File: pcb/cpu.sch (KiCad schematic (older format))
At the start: 36 parts, among them P27 BDM, P57 TX1, P58 RX1, P59 TX, P60 RX, P64 RXCAN0, P65 TXCAN0, U1 MC9S12XDP512, X1 16MHz

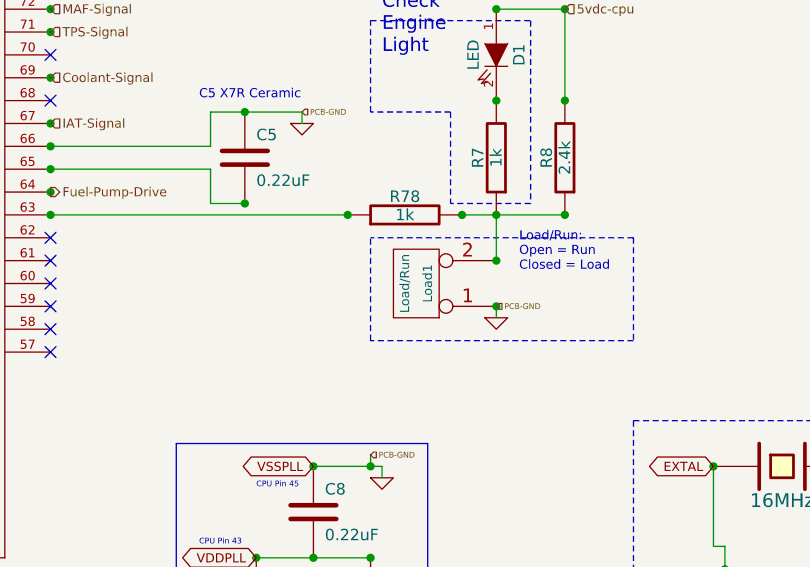
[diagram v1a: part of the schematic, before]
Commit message: Updated TODO.md for R20 and R23 footprint error.
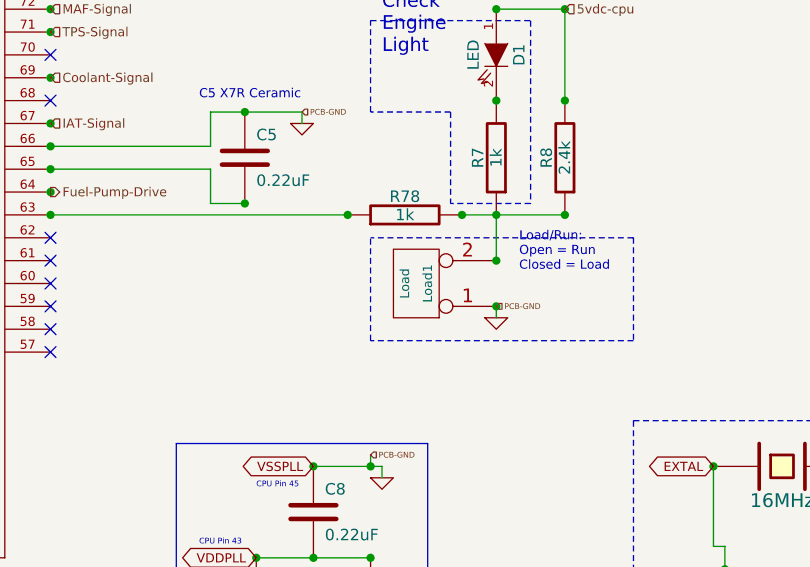
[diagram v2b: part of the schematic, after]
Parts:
- Load1: value Load/Run -> Load
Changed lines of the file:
@@
-EESchema Schematic File Version 2  date Sun 12 May 2013 04:07:09 PM EDT
+EESchema Schematic File Version 2  date Sun 12 May 2013 06:47:41 PM EDT
 LIBS:opto
 LIBS:power
@@
 Title "Jaguar PCB for FreeEMS"
 Date "12 may 2013"
-Rev "0.4-alpha"
-Comp "git hash: 3495ad36ad"
+Rev "0.6-alpha"
+Comp "git hash: xxxxxxxxxx"
 Comment1 ""
 Comment2 ""
@@
 P 8600 5150
 F 0 "Load1" V 8550 5150 40  0000 C CNN
-F 1 "Load/Run" V 8650 5150 40  0000 C CNN
+F 1 "Load" V 8650 5150 40  0000 C CNN
 	1    8600 5150
 	-1   0    0    1

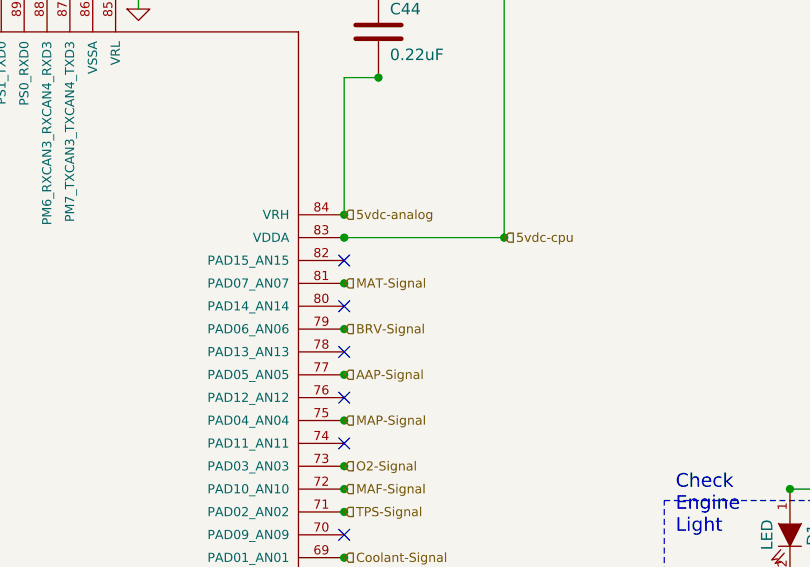
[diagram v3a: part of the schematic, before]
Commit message: Rename MAT to SPR.
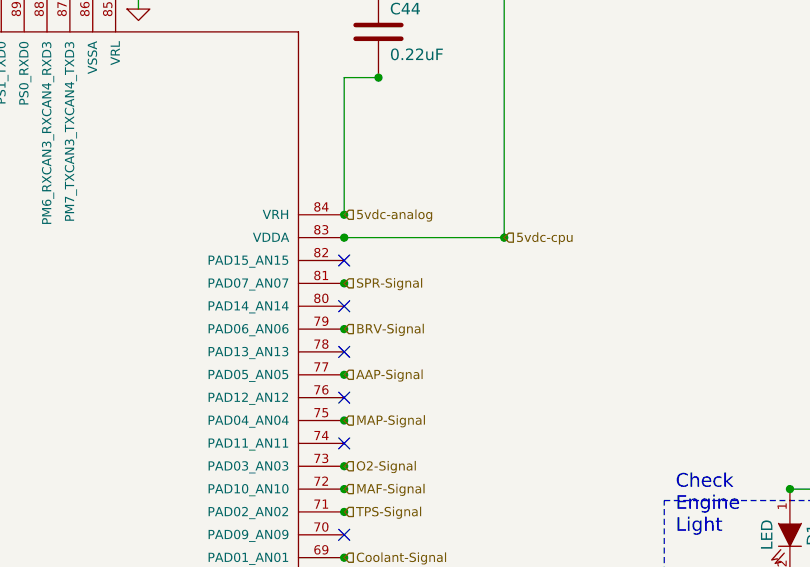
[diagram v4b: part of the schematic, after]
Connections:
- net labels added: SPR-Signal
- net labels removed: MAT-Signal
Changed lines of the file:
@@
-EESchema Schematic File Version 2  date Mon 13 May 2013 11:53:03 AM EDT
+EESchema Schematic File Version 2  date Mon 13 May 2013 12:23:58 PM EDT
 LIBS:opto
 LIBS:power
@@
 MAF-Signal
 Text HLabel 7000 3050 2    40   Input ~ 0
-MAT-Signal
+SPR-Signal
 Text HLabel 7000 3250 2    40   Input ~ 0
 BRV-Signal

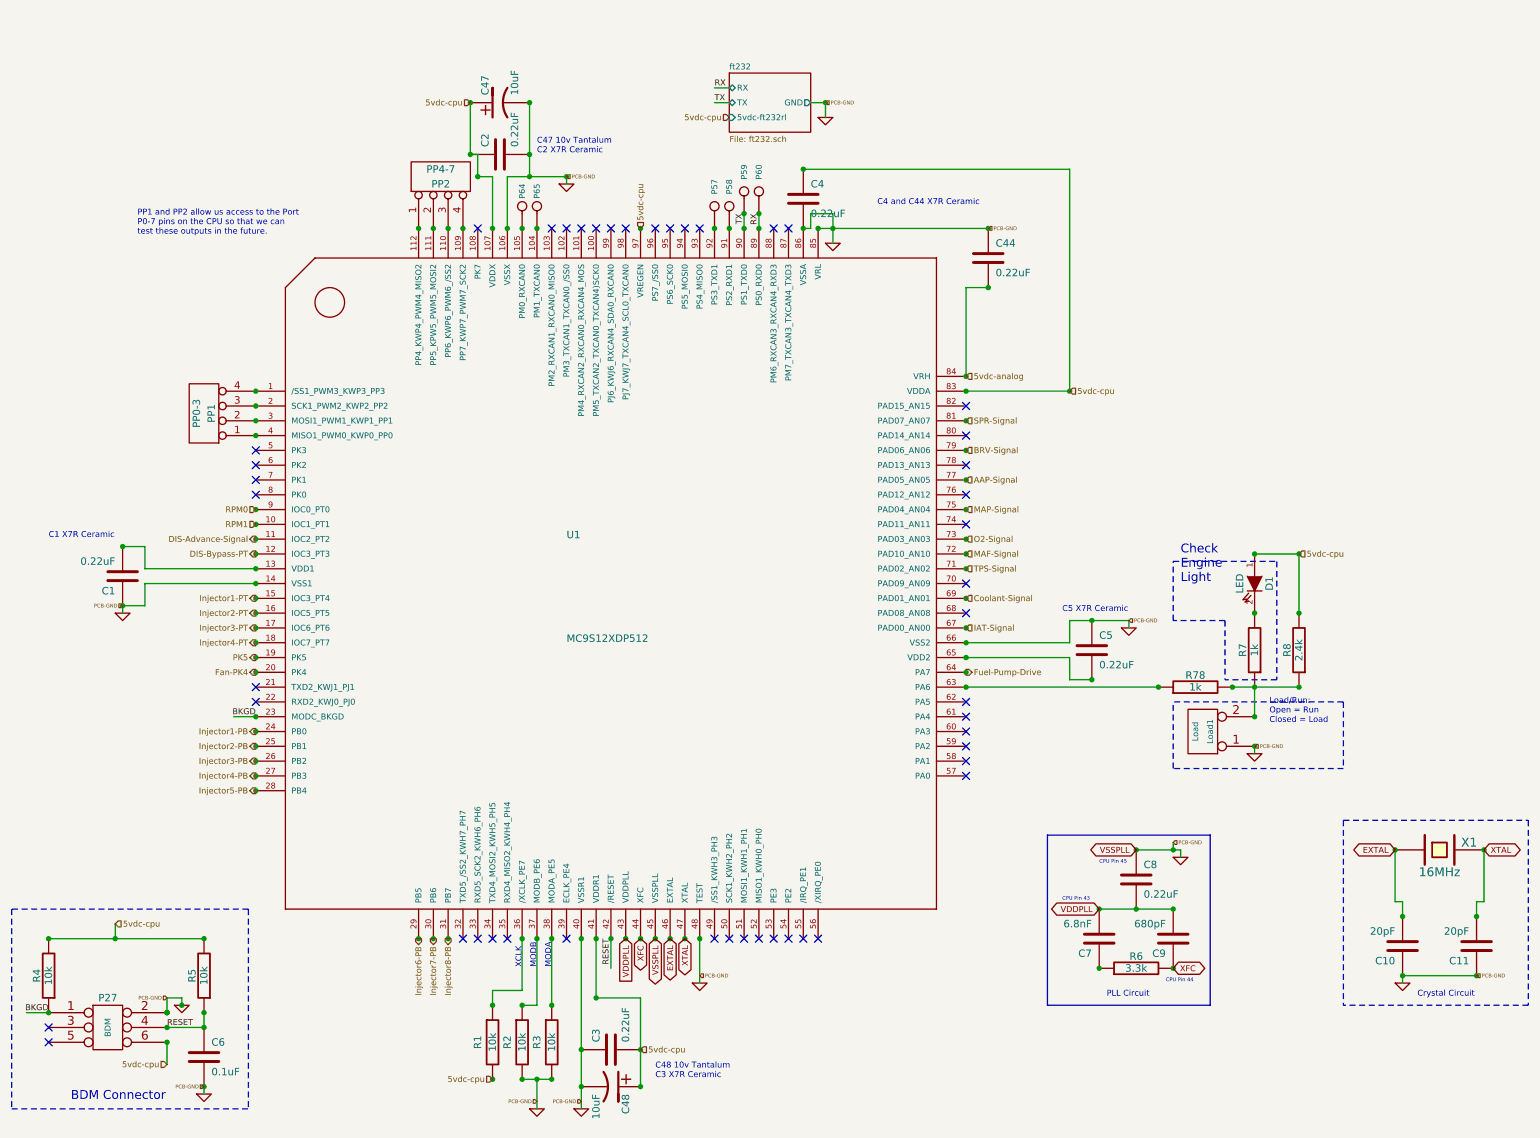
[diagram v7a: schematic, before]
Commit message: Made the CANRX0/CANTX0 into a 0.100" header so that a add-on card could be created later.
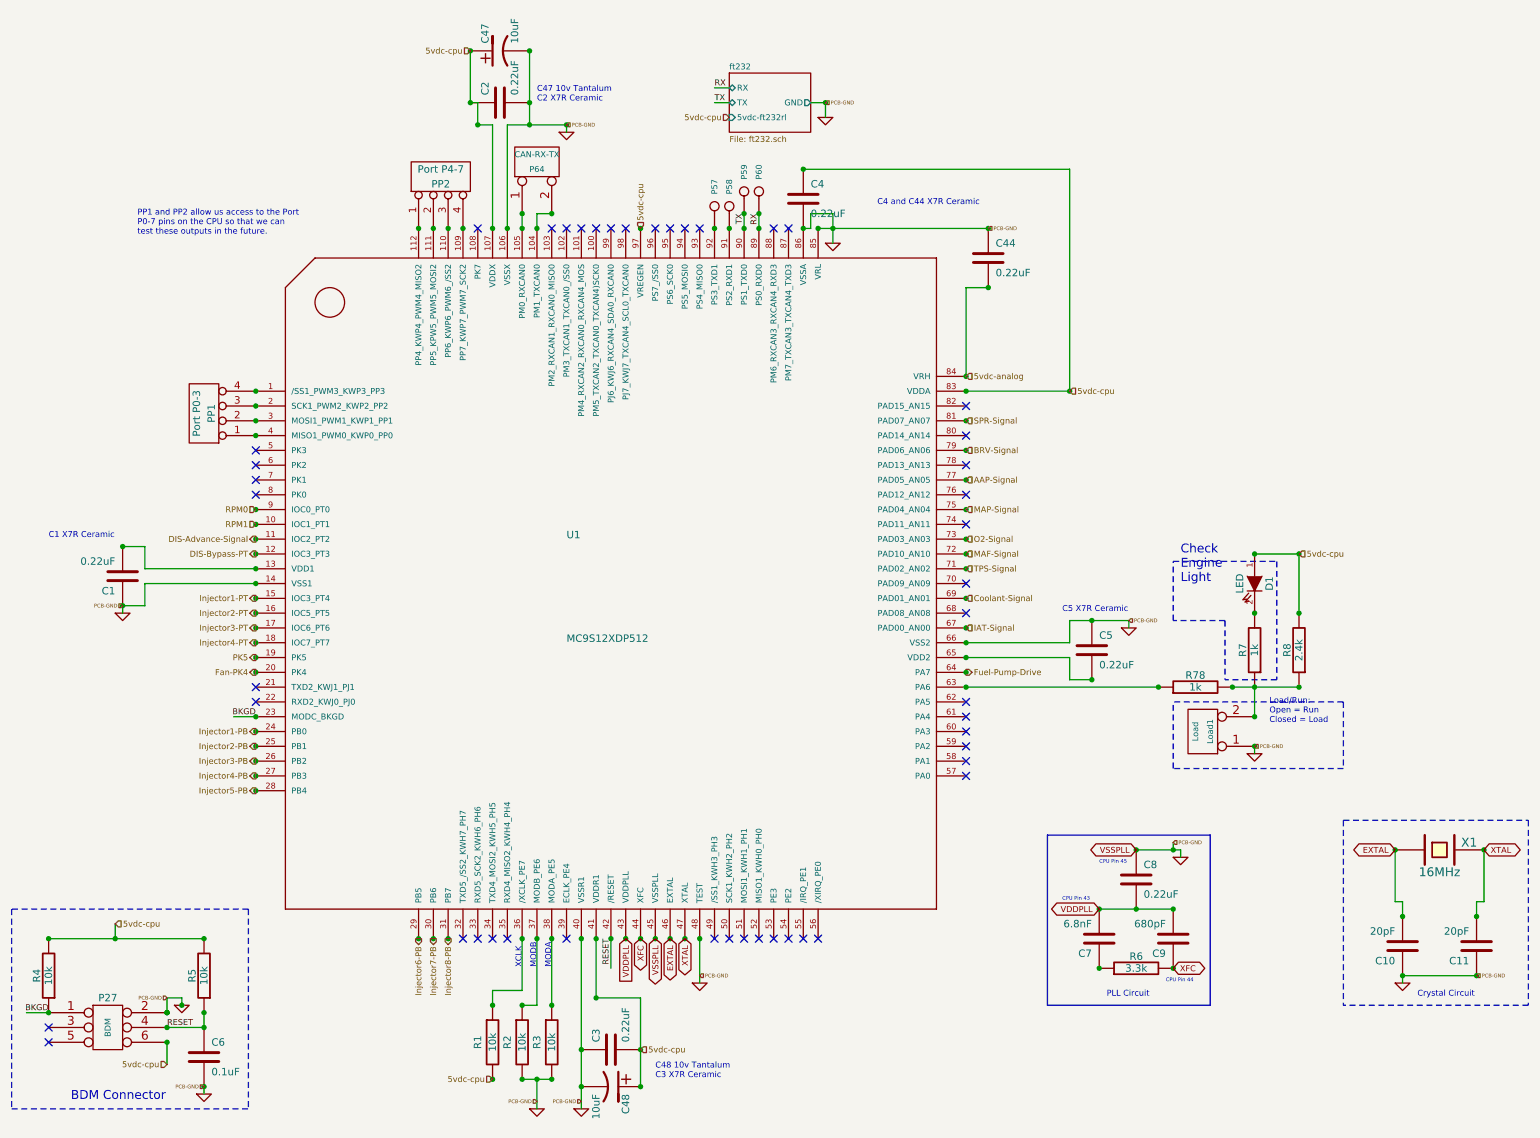
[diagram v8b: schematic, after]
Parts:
- removed P64: RXCAN0, symbol CONN_1
- removed P65: TXCAN0, symbol CONN_1
- added P64: CAN-RX-TX, symbol CONN_2
- PP1: value PP0-3 -> Port P0-3
- PP2: value PP4-7 -> Port P4-7
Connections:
- wire segments 82 -> 85
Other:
- moved on the sheet: C2, C47
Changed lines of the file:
@@
-EESchema Schematic File Version 2  date Wed 15 May 2013 02:06:49 PM EDT
+EESchema Schematic File Version 2  date Tue 21 May 2013 04:54:21 PM EDT
 LIBS:opto
 LIBS:power
@@
 Sheet 2 7
 Title "Jaguar PCB for FreeEMS"
-Date "15 may 2013"
+Date "21 may 2013"
 Rev "0.6-alpha"
 Comp "git hash: xxxxxxxxxx"
@@
 Comment4 ""
 $EndDescr
+Connection ~ 4200 1650
+Connection ~ 4000 1650
+Wire Wire Line
+	4000 1750 4000 1650
 Connection ~ 4100 1750
 Connection ~ 4000 1750
-Connection ~ 4300 1400
-Wire Wire Line
-	4300 1450 4300 1400
-Wire Wire Line
-	4050 1400 4050 900
+Connection ~ 4300 1050
+Wire Wire Line
+	4300 1100 4300 1050
+Wire Wire Line
+	4050 550  4050 1050
 Wire Wire Line
 	4100 7700 4100 7500
@@
 Wire Wire Line
 	1850 7550 1850 7600
-Connection ~ 4050 1400
-Wire Wire Line
-	4400 6550 4400 7700
+Connection ~ 4050 1050
+Wire Wire Line
+	4400 7700 4400 6550
 Wire Wire Line
 	4500 6950 4500 6550
@@
 Wire Wire Line
 	9250 3950 8950 3950
-Connection ~ 4050 1250
-Connection ~ 3650 1250
-Wire Wire Line
-	3900 1750 3900 1400
+Connection ~ 4050 900
+Connection ~ 3650 900
+Wire Wire Line
+	3900 1750 3900 1050
 Connection ~ 1300 3900
 Wire Wire Line
@@
 Connection ~ 1600 7050
 Wire Wire Line
-	7900 6350 8400 6350
+	8400 6350 7900 6350
 Wire Wire Line
 	10450 6300 10450 6400
@@
 	1450 4150 2200 4150
 Wire Wire Line
-	3800 1750 3800 1400
-Wire Wire Line
-	3800 1400 3700 1400
+	3800 1750 3800 1050
+Wire Wire Line
+	3800 1050 3700 1050
 Wire Wire Line
 	650  7050 800  7050
@@
 Connection ~ 800  6550
 Wire Wire Line
-	1850 6550 800  6550
+	800  6550 1850 6550
 Wire Notes Line
 	9550 5750 9550 7000
@@
 Wire Wire Line
 	7700 4800 7850 4800
-Connection ~ 3650 900
-Connection ~ 4050 900
+Connection ~ 3650 550
+Connection ~ 4050 550
 Connection ~ 4400 7300
 Connection ~ 4800 7300
@@
 	4200 6550 4200 7000
 Wire Wire Line
-	4200 7500 4000 7500
+	4000 7500 4200 7500
 Wire Wire Line
 	4000 6550 4000 6900
@@
 	9550 4950 8400 4950
 Wire Wire Line
-	3700 1250 3650 1250
-Wire Wire Line
-	3700 1250 3700 1400
-Connection ~ 3700 1400
-Wire Wire Line
-	3650 1250 3650 900
+	3700 900  3650 900
+Wire Wire Line
+	3700 900  3700 1050
+Connection ~ 3700 1050
+Wire Wire Line
+	3650 900  3650 550
 Connection ~ 3600 1750
 Connection ~ 3500 1750
@@
 	9100 4800 8750 4800
 Wire Wire Line
-	8800 4850 9250 4850
+	9250 4850 8800 4850
 Connection ~ 8800 4850
 Connection ~ 8300 4850
@@
 	6100 1650 6100 1850
 Wire Wire Line
-	7150 1750 6000 1750
+	6000 1750 7150 1750
 Connection ~ 5400 1750
 Connection ~ 5300 1750
@@
 Connection ~ 2200 4650
 Wire Wire Line
-	3900 1400 4300 1400
-$Comp
-L CONN_1 P65
-U 1 1 508EA553
-P 4100 1600
-F 0 "P65" H 4150 1600 40  0000 L CNN
-F 1 "TXCAN0" H 4100 1655 30  0001 C CNN
-	1    4100 1600
-	0    -1   -1   0
-$EndComp
-$Comp
-L CONN_1 P64
-U 1 1 508EA544
-P 4000 1600
-F 0 "P64" H 4050 1600 40  0000 L CNN
-F 1 "RXCAN0" H 4000 1655 30  0001 C CNN
-	1    4000 1600
+	3900 1050 4300 1050
+Wire Wire Line
+	4100 1750 4100 1650
+Wire Wire Line
+	4100 1650 4200 1650
+$Comp
+L CONN_2 P64
+U 1 1 519BDE3D
+P 4100 1300
+F 0 "P64" V 4050 1300 40  0000 C CNN
+F 1 "CAN-RX-TX" V 4150 1300 40  0000 C CNN
+	1    4100 1300
 	0    -1   -1   0
 $EndComp
@@
 Text HLabel 6050 900  2    25   Input ~ 0
 PCB-GND
-Text HLabel 4300 1400 2    25   Input ~ 0
+Text HLabel 4300 1050 2    25   Input ~ 0
 PCB-GND
 Text HLabel 9250 3950 2    40   Input ~ 0
@@
 L CP1 C47
 U 1 1 4F1E09CB
-P 3850 900
-F 0 "C47" H 3900 1000 50  0000 L CNN
-F 1 "10uF" H 3900 800 50  0000 L CNN
-	1    3850 900
+P 3850 550
+F 0 "C47" H 3900 650 50  0000 L CNN
+F 1 "10uF" H 3900 450 50  0000 L CNN
+	1    3850 550
 	0    -1   -1   0
 $EndComp
-Text HLabel 3650 900  0    40   Input ~ 0
+Text HLabel 3650 550  0    40   Input ~ 0
 5vdc-cpu
 Text Notes 7900 6050 0    25   ~ 0
@@
 P 3450 1400
 F 0 "PP2" V 3400 1400 50  0000 C CNN
-F 1 "PP4-7" V 3500 1400 50  0000 C CNN
+F 1 "Port P4-7" V 3500 1400 50  0000 C CNN
 	1    3450 1400
 	0    -1   -1   0
@@
 P 1850 3000
 F 0 "PP1" V 1800 3000 50  0000 C CNN
-F 1 "PP0-3" V 1900 3000 50  0000 C CNN
+F 1 "Port P0-3" V 1900 3000 50  0000 C CNN
 	1    1850 3000
 	-1   0    0    1
@@
 Text Notes 4900 7500 0    40   ~ 0
 C48 10v Tantalum\nC3 X7R Ceramic
-Text Notes 4100 1250 0    40   ~ 0
+Text Notes 4100 900  0    40   ~ 0
 C47 10v Tantalum\nC2 X7R Ceramic
 $Comp
@@
 L GND #PWR07
 U 1 1 4F1C289E
-P 4300 1450
-F 0 "#PWR07" H 4300 1450 30  0001 C CNN
-F 1 "GND" H 4300 1380 30  0001 C CNN
-	1    4300 1450
+P 4300 1100
+F 0 "#PWR07" H 4300 1100 30  0001 C CNN
+F 1 "GND" H 4300 1030 30  0001 C CNN
+	1    4300 1100
 	1    0    0    -1
 $EndComp
@@
 L C C2
 U 1 1 4F0A300F
-P 3850 1250
-F 0 "C2" H 3900 1350 50  0000 L CNN
-F 1 "0.22uF" H 3900 1150 50  0000 L CNN
-	1    3850 1250
+P 3850 900
+F 0 "C2" H 3900 1000 50  0000 L CNN
+F 1 "0.22uF" H 3900 800 50  0000 L CNN
+	1    3850 900
 	0    -1   -1   0
 $EndComp
